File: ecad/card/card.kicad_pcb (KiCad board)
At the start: 4 copper layers, 133.4 x 32.2 mm, 136 parts, among them J1 Conn_01x03_Pin, J2 USB4105-GF-A, J3 10145226-0241N13LF, J4 Conn_01x03_Pin, J5 Conn_01x03_Pin, SW1 TS-1187A-B-A-B, SW2 TS-1187A-B-A-B, U1 W25Q128JVS, U2 RP2350_80QFN, U3 MCP23017_SO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

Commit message: production fixups
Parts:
- U2: value RP2350_80QFN -> RP2350B
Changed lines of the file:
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@@
 		(sheetname "Root")
 		(sheetfile "card.kicad_sch")
-		(attr smd)
+		(attr smd dnp)
 		(fp_line
 			(start -3.86 -9.06)
@@
 			)
 		)
-		(property "Value" "RP2350_80QFN"
+		(property "Value" "RP2350B"
 			(at 0 6.549999 45)
 			(layer "F.Fab")
@@
 		(sheetname "Root")
 		(sheetfile "card.kicad_sch")
-		(attr smd)
+		(attr smd dnp)
 		(fp_line
 			(start -3.86 -9.06)
@@
 			(at 0 0 -135)
 			(unlocked yes)
+			(layer "F.Fab")
+			(hide yes)
+			(effects
+				(font
+					(size 1 1)
+					(thickness 0.15)
+				)
+			)
+		)
+		(property "LCSC Part #" "C42411119"
+			(at 0 0 -135)
+			(unlocked yes)

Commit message: Files for JLCPCB
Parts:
- C21: footprint Capacitor_SMD:C_0402_1005Metric -> Capacitor_SMD:C_0805_2012Metric_Pad1.18x1.45mm_HandSolder
- R10, R9: footprint Resistor_SMD:R_0402_1005Metric -> Resistor_SMD:R_0603_1608Metric_Pad0.98x0.95mm_HandSolder
- R5, R6: footprint Capacitor_SMD:C_0603_1608Metric_Pad1.08x0.95mm_HandSolder -> Resistor_SMD:R_0603_1608Metric_Pad0.98x0.95mm_HandSolder
- R7: footprint Resistor_SMD:R_0402_1005Metric -> Resistor_SMD:R_0805_2012Metric_Pad1.20x1.40mm_HandSolder
- moved C21 2.46 mm to (87.2, 64.7), turned to -45 degrees
- moved R7 0.65 mm to (91.9, 56.0)
- moved R10 0.27 mm to (65.3, 55.6)
- moved R9 0.17 mm to (53.7, 54.1)
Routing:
- net /~{RESET}: track 135.1 -> 136.9 mm
- net GND: track 216.5 -> 217.6 mm
- net 3.3V: track 227.3 -> 227.9 mm
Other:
- board text added: "rev. 01 3/17/2025"
- board text removed: "rev. 01 3/14/2025"

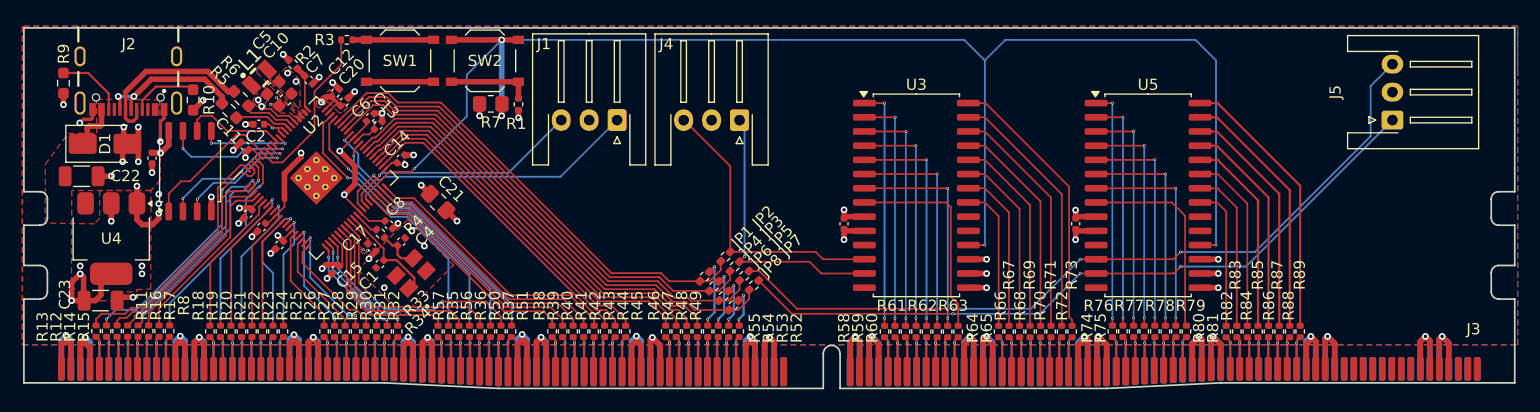
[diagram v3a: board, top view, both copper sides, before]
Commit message: increase via sizes
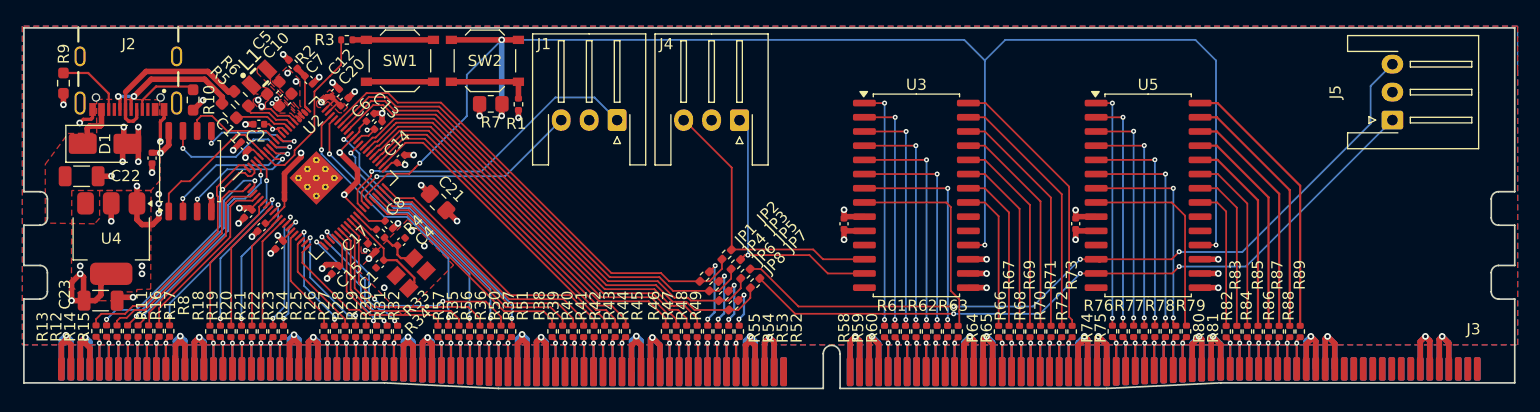
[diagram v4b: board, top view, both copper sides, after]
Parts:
- moved JP5 0.21 mm to (114.7, 71.1)
- moved JP7 0.21 mm to (115.5, 72.0)
- moved JP2 0.21 mm to (113.0, 69.4)
- moved JP3 0.21 mm to (113.8, 70.3)
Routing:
- net Net-(U1-DI(IO0)): track 8.45 -> 10.7 mm
- net Net-(U1-IO3): track 12.2 -> 14.1 mm
- net Net-(J1-Pin_1): track 28.0 -> 29.6 mm
- net /ADDR05: track 8.97 -> 10.6 mm
- net /ADDR07: track 10.7 -> 12.3 mm
- net /ADDR06: track 9.71 -> 11.3 mm
- net Net-(U1-DO(IO1)): track 12.7 -> 14.1 mm
- net Net-(U1-IO2): track 11.1 -> 12.0 mm
- net /I2C1_SCL: track 70.7 -> 69.9 mm
- net /DATA06: track 12.0 -> 11.2 mm
- net 3.3V: track 227.9 -> 228.2 mm, vias 41 -> 40
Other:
- board text added: "rev. 01 3/18/2025"
- board text removed: "rev. 01 3/17/2025"

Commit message: enlarge holes to 0.3mm
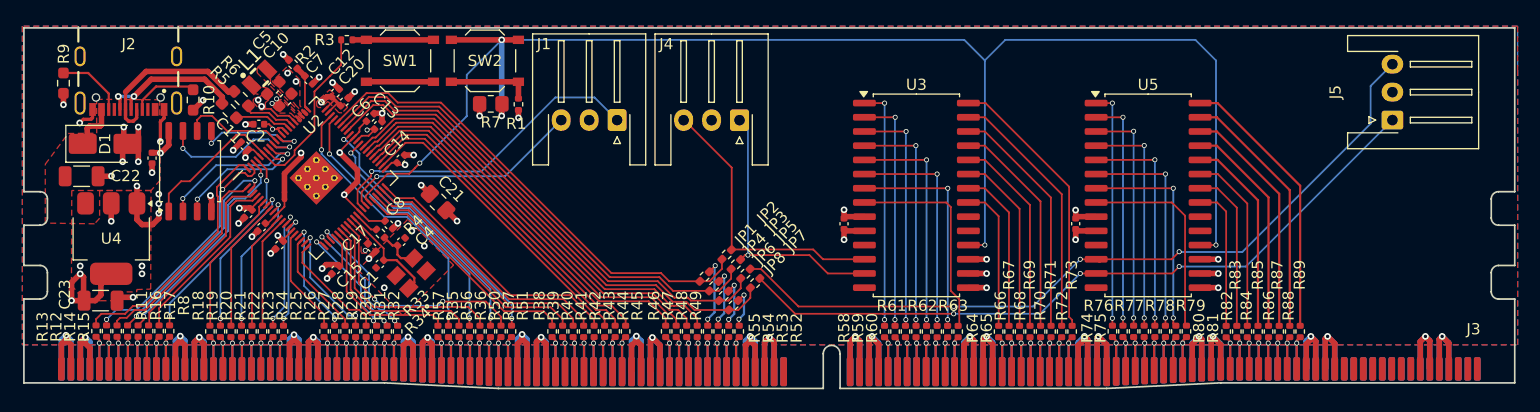
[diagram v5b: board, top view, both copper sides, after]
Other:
- board text added: "rev. 01 3/20/2025"
- board text removed: "rev. 01 3/18/2025"
